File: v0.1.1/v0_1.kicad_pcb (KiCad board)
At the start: 2 copper layers, 110 x 70 mm, 31 parts

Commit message: moved components
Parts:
- moved Battery 33.0 mm to (244.7, 92.7)
- moved Accelerometer 20.3 mm to (215.9, 87.8)
- moved C6 20.3 mm to (209.2, 82.2)
- moved C7 20.3 mm to (213.7, 82.2)
- moved C8 20.3 mm to (218.2, 82.2)
- moved C9 20.3 mm to (222.7, 82.2)
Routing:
- net /vACC: track 278.0 -> 249.2 mm
- net /X_ACC: track 84.1 -> 56.1 mm, vias 4 -> 0
- net /Z_ACC: track 90.0 -> 62.8 mm, vias 6 -> 0
- net /Y_ACC: track 88.4 -> 63.3 mm, vias 6 -> 0
- net /vBAT: track 60.1 -> 44.6 mm, vias 2 -> 0
- net Net-(MCU1-PA31): vias 4 -> 0
- net Net-(MCU1-PA30): vias 4 -> 0
- net Net-(MCU1-PA00): vias 2 -> 0
- net GND: vias 1127 -> 0
- net /SDA: vias 4 -> 0
- net /SCLK_SD: vias 2 -> 0
- net /SCLK: vias 4 -> 0
- net /PPG_V: vias 6 -> 0
- net /PPG: vias 6 -> 0
- net /MOSI_SD: vias 4 -> 0
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
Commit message: White Boxes
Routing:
- net /vACC: track 249.2 -> 266.9 mm, vias 0 -> 2
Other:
- board text added: "LR"
- board text added: "MPU"
- board text added: "MicroSD"
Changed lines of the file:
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@@
 		(tags "test point SMD pad")
 		(property "Reference" "SWCLK"
-			(at 0 -5 180)
+			(at 2.75 0 180)
 			(layer "F.SilkS")
 			(effects
@@
 		(tags "test point SMD pad")
 		(property "Reference" "SWDIO"
-			(at 0 -5 180)
+			(at -2.5 0 180)
 			(layer "F.SilkS")
 			(effects
@@
 		(tags "LFCSP 16 0.65")
 		(property "Reference" "Accelerometer"
-			(at 0.145 -4.5 0)
+			(at -0.3 -6.75 0)
 			(layer "F.SilkS")
 			(effects
 				(font
-					(size 1 1)
-					(thickness 0.15)
+					(size 2 2)
+					(thickness 0.3)
 				)
 			)
@@
 		(tags "NCP711ASN330T1G ")
 		(property "Reference" "Linear Regulator"
-			(at -0.06 9.25 0)
+			(at -14.06 7 0)
 			(unlocked yes)
 			(layer "F.SilkS")
 			(effects
 				(font
-					(size 1 1)
-					(thickness 0.15)
+					(size 2 2)
+					(thickness 0.3)
 				)
 			)
@@
 		(tags "SOIC SO")
 		(property "Reference" "Real-time Clock"
-			(at 0.05 -3.6925 0)
+			(at 0.5 6.3075 0)
 			(layer "F.SilkS")
 			(effects
 				(font
-					(size 1 1)
-					(thickness 0.15)
+					(size 2 2)
+					(thickness 0.3)
 				)
 			)
@@
 			(unlocked yes)
 			(layer "F.SilkS")
+			(hide yes)
 			(effects
 				(font
@@
 			(effects
 				(font
-					(size 1 1)
-					(thickness 0.15)
+					(size 2 2)
+					(thickness 0.3)
 				)
 			)
@@
 			(effects
 				(font
-					(size 1 1)
-					(thickness 0.15)
+					(size 2 2)
+					(thickness 0.3)
 				)
 			)
@@
 		(layer "F.SilkS")
 	)
+	(gr_rect
+		(start 205 78.5)
+		(end 227.75 93)
+		(stroke
+			(width 0.1)
+			(type default)
+		)
+		(fill no)
+		(layer "F.SilkS")
+	)
 	(gr_line
 		(start 237.8 106.1)
@@
 		(layer "F.SilkS")
 	)
+	(gr_rect
+		(start 152 103.75)
+		(end 163.25 124.5)
+		(stroke
+			(width 0.1)
+			(type default)
+		)
+		(fill no)
+		(layer "F.SilkS")
+	)
 	(gr_line
 		(start 206.15 116.205)
@@
 		(layer "F.SilkS")
 	)
+	(gr_rect
+		(start 232.25 86.25)
+		(end 256.5 113.25)
+		(stroke
+			(width 0.1)
+			(type default)
+		)
+		(fill no)
+		(layer "F.SilkS")
+	)
 	(gr_line
 		(start 159.3 105.4)
@@
 		(layer "F.SilkS")
 	)
+	(gr_rect
+		(start 188.25 97.5)
+		(end 219 120.25)
+		(stroke
+			(width 0.1)
+			(type default)
+		)
+		(fill no)
+		(layer "F.SilkS")
+	)
 	(gr_line
 		(start 250.25 112.7)
@@
 	)
 	(gr_text "Microprocessor"
-		(at 203 116.95 0)
+		(at 203.25 122 0)
+		(layer "F.SilkS")
+		(effects
+			(font
+				(size 2 2)
+				(thickness 0.3)
+			)
+		)
+	)
+	(gr_text "LR\n"
+		(at 161 113 0)
 		(layer "F.SilkS")
 		(effects
@@
 		)
 	)
+	(gr_text "MicroSD"
+		(at 232.5 127.5 0)
+		(layer "F.SilkS")
+		(effects
+			(font
+				(size 2 2)
+				(thickness 0.3)
+			)
+		)
+	)
+	(gr_text "MPU"
+		(at 203 117.5 0)
+		(layer "F.SilkS")
+		(effects
+			(font
+				(size 1 1)
+				(thickness 0.15)
+			)
+		)
+	)
 	(gr_text "Edge Computing Power \nManagement Development Kit\n"
-		(at 211.95 143.4 0)
+		(at 212.5 143.4 0)
 		(layer "F.SilkS")
 		(effects
@@
 	)
 	(segment
+		(start 223.98375 105.11625)
+		(end 226.85 102.25)
+		(width 0.3)
+		(layer "F.Cu")
+		(net 3)
+	)
+	(segment
 		(start 242 102.175)
 		(end 244.225 102.175)
@@
 	)
 	(segment
+		(start 238 102.25)
+		(end 240.4 102.25)
+		(width 0.3)
+		(layer "F.Cu")
+		(net 3)
+	)
+	(segment
 		(start 195.5 122.6)
 		(end 183.5 122.6)
@@
 	)
 	(segment
+		(start 226.85 102.25)
+		(end 236 102.25)
+		(width 0.3)
+		(layer "F.Cu")
+		(net 3)
+	)
+	(segment
 		(start 252.2 107.55)
 		(end 252.2 110.8)
@@
 	)
 	(segment
+		(start 240.4 102.25)
+		(end 240.475 102.175)
+		(width 0.3)
+		(layer "F.Cu")
+		(net 3)
+	)
+	(segment
 		(start 223.98375 105.11625)
 		(end 223.8675 105)
@@
 		(net 3)
 	)
+	(via
+		(at 238 102.25)
+		(size 0.6)
+		(drill 0.3)
+		(layers "F.Cu" "B.Cu")
+		(net 3)
+	)
+	(via
+		(at 236 102.25)
+		(size 0.6)
+		(drill 0.3)
+		(layers "F.Cu" "B.Cu")
+		(net 3)
+	)
+	(segment
+		(start 236 102.25)
+		(end 238 102.25)
+		(width 0.3)
+		(layer "B.Cu")
+		(net 3)
+	)

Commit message: Ground plane
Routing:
- net GND: track 28.1 -> 47.0 mm, vias 0 -> 881
- net /vACC: track 266.9 -> 281.2 mm
- net /D+: track 51.5 -> 53.4 mm, vias 0 -> 2
- net /SCLK: track 45.1 -> 45.4 mm, vias 0 -> 4
- net Net-(MCU1-PA31): vias 0 -> 4
- net Net-(MCU1-PA30): vias 0 -> 4
- net Net-(MCU1-PA00): vias 0 -> 2
- net /Z_ACC: vias 0 -> 6
- net /Y_ACC: vias 0 -> 6
- net /X_ACC: vias 0 -> 4
- net /SDA: vias 0 -> 4
- net /SCLK_SD: vias 0 -> 2
- net /PPG_V: vias 0 -> 6
- net /PPG: vias 0 -> 6
- net /MOSI_SD: vias 0 -> 4
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
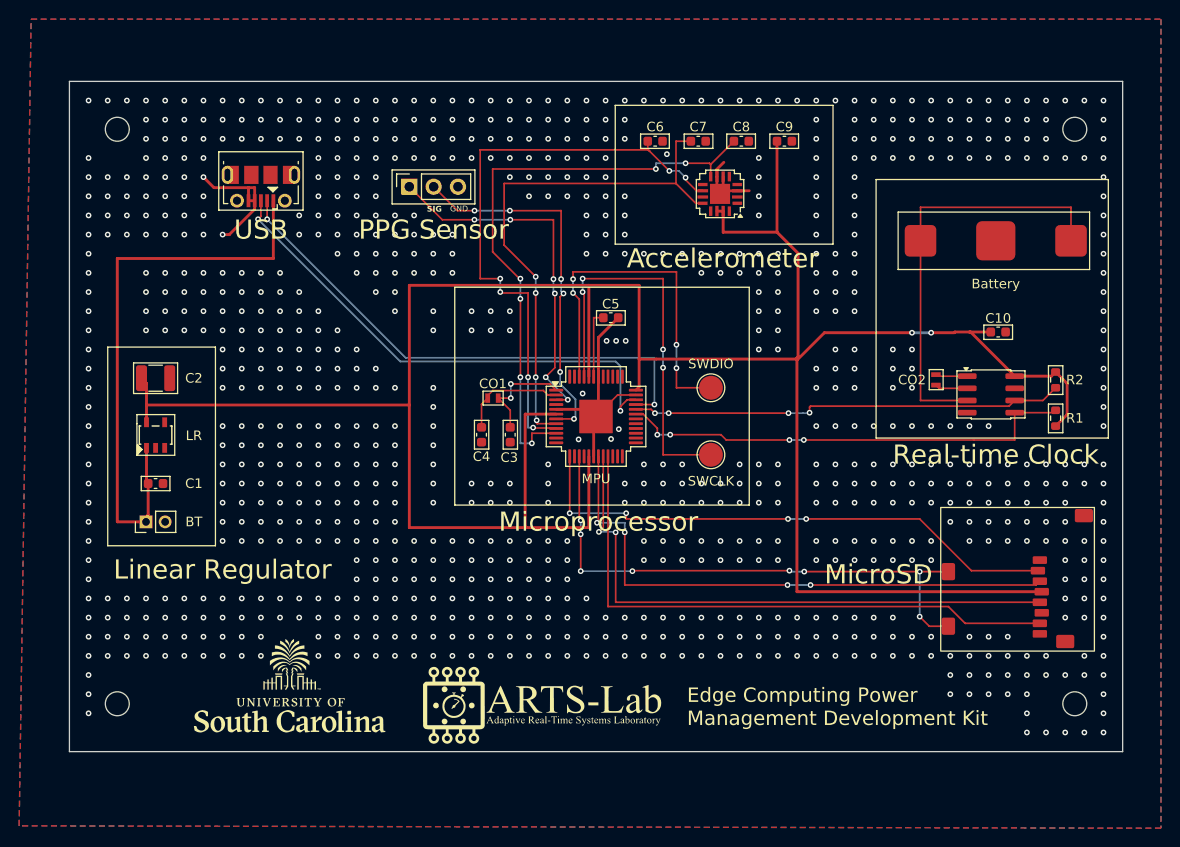
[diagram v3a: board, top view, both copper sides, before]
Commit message: Moved resistors
Now they are connected properly to SDA, SCL, and VCC.
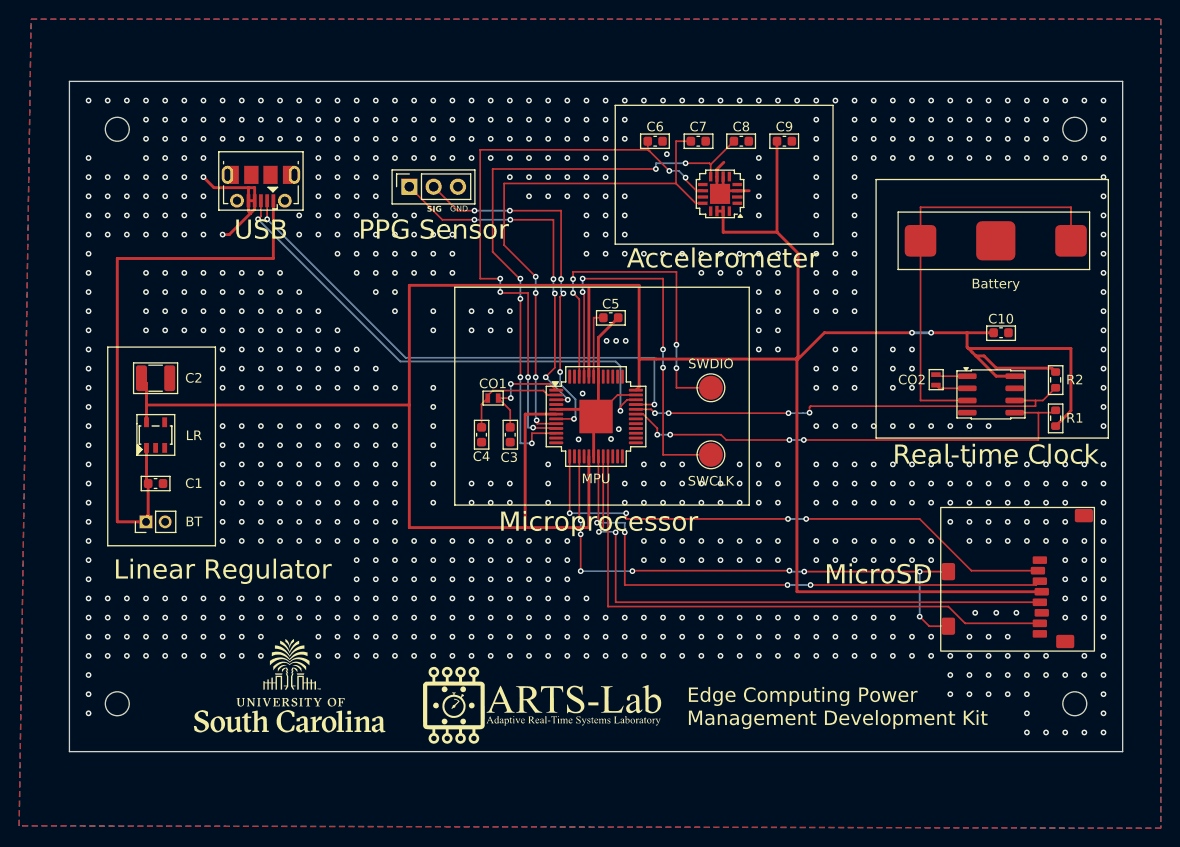
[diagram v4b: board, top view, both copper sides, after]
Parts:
- moved C10 0.31 mm to (245.3, 102.2)
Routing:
- net /vACC: track 281.2 -> 299.9 mm
- net /SCLK: track 45.4 -> 48.0 mm
- net /SDA: track 48.3 -> 50.8 mm
- net GND: track 47.0 -> 48.4 mm, vias 881 -> 884
